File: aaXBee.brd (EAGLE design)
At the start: 100 x 80 mm, 67 parts, among them Q1 IRLML6244TR, U1 MCP1640C, U2 ATmega328P-AU, U3 DS3232, X1 XB24-Z7WIT-004, Y2 8MHz

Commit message: First reasonably complete routing.
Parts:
- removed C10: 27pF, _jc:M0805
- removed D2: Green, adafruit:CHIPLED_1206
- removed JMP1: solder jumper, _jc:M0805
- removed JP4: RTC BACKUP, SparkFun:1X03_LOCK
- removed R8: 1K, _jc:M0805
- removed S1: RESET, _jc:SWITCH-TACT-6X3.5-SMT
- removed U3: DS3232, _jc:SO20W
- removed X1: XB24-Z7WIT-004, _jc:XBEE_OVAL_PADS
- removed Y2: 8MHz, _jc:CRYSTAL-ABRACON-ABM2
- added A1: XB24-Z7WIT-004, _jc:XBEE_OVAL_PADS
- added B2: 2xAA, _jc:KEYSTONE-2462-NO-HOLES
- added C12, C13: 100nF, _jc:M0805
- added C14, C16: 27pF, _jc:M0805
- added L2: 10uH, _jc:M0805
- added L3: 4.7uH, _jc:NRS4018
- added PR14, PR15, PR16, PR17: PROTO-10, _jc:PROTO-10
- added R16: 562K, _jc:M0805
- added R17: 249K, _jc:M0805
- added SJ1: 5V, jumper:SJ
- added SJ2: (no value), jumper:SJ_2
- added SJ3: 3V3, jumper:SJ
- added SW1: (no value), _jc:SWITCH-TACT-6X3.5-SMT
- added SW2: RESET, _jc:SWITCH-TACT-6X3.5-SMT
- added U4: ATmega328P-AU, atmel:TQFP32-08
- added U5: MCP9808, _jc:MSOP8
- added U6: DS3231, _jc:SO-16DW
- added Y1: 8MHz, _jc:CRYSTAL-ABRACON-ABM2
- C15: value 10uF -> 100nF; device _jc:C0805 -> _jc:M0805
- C6, C7: value 100nF -> 10uF
- C9: value 27pF -> 100nF
- D1: value Red -> Yellow; device adafruit:CHIPLED_1206 -> _jc:D0805
- D7, D8: device adafruit:CHIPLED_0805 -> _jc:D0805
- R13, R14, R15: device _jc:R0805 -> _jc:M0805
- R3: value 249K -> 976K
- U1: value MCP1640C -> MCP1640D
- U2: value ATmega328P-AU -> MCP1640D; device atmel:TQFP32-08 -> _jc:SOT23-6
- moved LOGO1 170.6 mm to (90.2, 68.6)
- moved U$2 162.3 mm to (96.5, 30.5), turned to 90 degrees
- moved PR13 161.4 mm to (86.4, 57.1)
- moved JP6 149.6 mm to (63.5, 3.81)
- moved PR2 145.5 mm to (82.5, 21.6)
- moved PR12 143.4 mm to (82.5, 47.0)
- moved PR10 143.0 mm to (82.5, 44.5)
- moved PR8 142.6 mm to (82.5, 41.9)
- moved PR6 142.2 mm to (82.5, 39.4)
- moved PR4 141.8 mm to (82.5, 36.8)
- moved R5 140.7 mm to (57.1, 27.9), turned to 270 degrees
- moved C4 139.4 mm to (59.7, 27.9), turned to 270 degrees
- moved Q1 138.6 mm to (80.0, 3.81), turned to 270 degrees
- moved C5 136.1 mm to (49.5, 17.4), turned to 270 degrees
- moved R12 133.0 mm to (74.9, 3.81), turned to 180 degrees
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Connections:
- removed net LED2: R8.2, U2.12
- removed net N$11: C10.1, U2.8, Y2.P$1
- removed net N$3: D2.A, R8.1
- removed net N$39: R14.2, X1.6
- removed net N$40: R15.2, X1.15
- new net AREF: C13.1, JP1.1, U4.20
- new net ASC: A1.15, R15.2
- new net CTS: A1.12, U4.9
- new net N$43: C14.1, U4.7, Y1.P$2
- new net N$44: C16.1, U4.8, Y1.P$1
- new net N$46: C12.1, L2.2, U4.18
- new net RSSI: A1.6, R14.2
- new net SLP: A1.9, U4.10
- new net SW1: SW1.P$1, U4.12
- net +3V3: now also C7.1, R3.1, SJ2.1, U2.5; no longer C15.1, R13.1, X1.1
- net /RESET: now also SW2.P$1, U4.29; no longer S1.P$1, U2.29
- net /SS: now also JP1.12, U4.14; no longer JP1.9, U2.14
- net 32KHZ: now also U6.1; no longer JP1.1, U3.3
- net ADC0: now also U4.23; no longer U2.23
- net ADC1: now also U4.24; no longer U2.24
- net ADC2: now also U4.25; no longer U2.25
- net ADC3: now also U4.26; no longer U2.26
- net ADC6: now also U4.19; no longer U2.19
- net ADC7: now also U4.22; no longer U2.22
- net BAT: now also B2.POS, C6.1, L3.P$1, U2.6; no longer JP4.1
- net EN: now also U2.3, U4.2; no longer U2.2
- net GND: now also A1.10, B2.NEG, C12.2, C13.2, C14.2, C16.2, D1.K, D7.K, D8.K, R16.2, R17.2, SJ1.2, SW1.P$2, SW2.P$2, U2.2, U4.21, U4.3, U4.5, U5.4, U5.5, U5.6, U5.7, U6.10, U6.11, U6.12, U6.13, U6.5, U6.6, U6.7, U6.8, U6.9; no longer C10.2, D1.C, D2.C, D7.C, D8.C, JMP1.2, R3.2, S1.P$2, U2.21, U2.3, U2.5, U3.1, U3.10, U3.11, U3.12, U3.13, U3.14, U3.15, U3.19, U3.2, U3.7, U3.8, U3.9, X1.10
- net INT: now also U4.1, U6.3; no longer U2.1, U3.5
- net LED1: now also U4.11; no longer U2.11
- net MISO: now also JP1.10, U4.16; no longer JP1.11, U2.16
- net MOSI: now also JP1.11, U4.15; no longer JP1.12, U2.15
- net N$1: now also U6.14; no longer JP4.3
- net N$12: now also R16.1, R3.2, U2.4; no longer JMP1.1, R2.2, R3.1
- net N$13: now also L3.P$2, U2.1; no longer C8.1, U2.20
- net N$35: now also A1.1, C15.1, C3.1, R13.1, SJ2.2; no longer JP4.2, U3.16
- net N$37: now also A1.3, SJ3.1; no longer X1.3
- net N$38: now also A1.2; no longer X1.2
- net N$8: now also R17.1, R2.2, SJ1.1; no longer C9.1, U2.7, Y2.P$2
- net PPWR: now also C9.1, U4.32, U5.8, U6.2; no longer U2.32, U3.4
- net RXD: now also U4.30; no longer U2.30
- net SCK: now also JP1.9, U4.17; no longer JP1.10, U2.17
- net SCL: now also R10.2, U4.28, U5.2, U6.16; no longer R10.1, U2.28, U3.18
- net SDA: now also R9.2, U4.27, U5.1, U6.15; no longer R9.1, U2.27, U3.17
- net SPWR: now also U4.13; no longer U2.13
- net TXD: now also SJ3.2, U4.31; no longer U2.31
- net VCC: now also C8.1, L2.1, R10.1, R9.1, SJ2.3, U4.4, U4.6; no longer C3.1, C6.1, C7.1, R10.2, R9.2, U2.18, U2.4, U2.6
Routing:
- net VCC: track 0.00 -> 86.0 mm, vias 0 -> 9
- net BAT: track 0.00 -> 80.2 mm, vias 0 -> 1
- net /RESET: track 0.00 -> 60.1 mm, vias 0 -> 2
- net SDA: track 0.00 -> 54.5 mm, vias 0 -> 3
- net SPWR: track 0.00 -> 53.5 mm, vias 0 -> 2
- net SCK: track 0.00 -> 49.0 mm
- net EN: track 0.00 -> 48.7 mm, vias 0 -> 3
- net SCL: track 0.00 -> 48.6 mm, vias 0 -> 2
- net SGND: track 0.00 -> 47.2 mm
- net RXD: track 0.00 -> 45.3 mm, vias 0 -> 1
- net TXD: track 0.00 -> 43.2 mm, vias 0 -> 1
- net MISO: track 0.00 -> 41.6 mm
- net SLP: track 0.00 -> 39.9 mm, vias 0 -> 1
- net MOSI: track 0.00 -> 38.0 mm
- net ADC7: track 0.00 -> 37.7 mm, vias 0 -> 3
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- added copper zone on layer 1, net GND
- added copper zone on layer 16, net VCC
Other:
- board size 100 x 80 mm -> 99.1 x 61 mm
- board text added: "+3V-"

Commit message: Routing complete.
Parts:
- removed JP1: PROTO-12NR, _jc:PROTO-12-NR
- removed U$1, U$2: PROTO-12PROTO, _jc:PROTO-12
- added PR18, PR19: (no value), _jc:PROTO-16
- added PR20: (no value), _jc:PROTO-14-NR
- added SJ4: 5V, jumper:SJ
- SJ3: value 3V3 -> /5V
- moved R4 23.6 mm to (12.3, 55.9)
- moved TB1 17.4 mm to (6.60, 49.1)
- moved D1 12.8 mm to (58.4, 3.81)
- moved R7 12.8 mm to (58.4, 8.89)
- moved SW2 11.9 mm to (45.2, 6.48)
- moved R10 11.4 mm to (66.0, 55.9)
- moved B1 11.4 mm to (29.2, 50.8)
- moved C11 11.4 mm to (55.9, 55.9)
- moved C9 11.4 mm to (58.4, 55.9)
- moved R9 11.4 mm to (68.6, 55.9)
- moved U5 11.4 mm to (62.2, 55.9)
- moved U6 11.4 mm to (48.3, 53.3)
- moved D4 6.35 mm to (27.9, 14.0), turned to 90 degrees
- moved C5 4.73 mm to (44.8, 16.9), turned to 180 degrees
- moved R6 3.82 mm to (48.6, 16.0)
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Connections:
- net +3V3 renamed N$39
- net N$35 renamed XBEE_SUPPLY
- removed net LED1: R7.2, U4.11
- removed net SW1: SW1.P$1, U4.12
- new net N$35: C6.1, L3.P$1, SJ4.2, U2.6
- new net N$40: PR14.1, PR14.2, PR14.3, PR14.4, PR14.5
- new net N$45: PR14.10, PR14.6, PR14.7, PR14.8, PR14.9
- new net N$47: PR15.1, PR15.2, PR15.3, PR15.4, PR15.5
- new net N$48: PR15.10, PR15.6, PR15.7, PR15.8, PR15.9
- new net N$49: PR16.1, PR16.2, PR16.3, PR16.4, PR16.5
- new net N$50: PR16.10, PR16.6, PR16.7, PR16.8, PR16.9
- new net N$51: PR17.1, PR17.2, PR17.3, PR17.4, PR17.5
- new net N$52: PR17.10, PR17.6, PR17.7, PR17.8, PR17.9
- new net PB0: R7.2, U4.12
- new net PD7: SW1.P$1, U4.11
- net /SS: now also PR20.3; no longer JP1.12
- net ADC0: now also PR20.9; no longer JP1.7
- net ADC1: now also PR20.10; no longer JP1.6
- net ADC2: now also PR20.11; no longer JP1.5
- net ADC3: now also PR20.12; no longer JP1.4
- net ADC6: now also PR20.7; no longer JP1.8
- net AREF: now also PR20.8; no longer JP1.1
- net BAT: now also SJ4.1; no longer C6.1, L3.P$1, U2.6
- net MISO: now also PR20.5; no longer JP1.10
- net MOSI: now also PR20.4; no longer JP1.11
- net SCK: now also PR20.6; no longer JP1.9
- net SCL: now also PR20.14; no longer JP1.2
- net SDA: now also PR20.13; no longer JP1.3
- net SGND: now also PR18.1, PR18.10, PR18.11, PR18.12, PR18.13, PR18.14, PR18.15, PR18.16, PR18.2, PR18.3, PR18.4, PR18.5, PR18.6, PR18.7, PR18.8, PR18.9; no longer U$2.1, U$2.10, U$2.11, U$2.12, U$2.2, U$2.3, U$2.4, U$2.5, U$2.6, U$2.7, U$2.8, U$2.9
- net VCC: now also PR19.1, PR19.10, PR19.11, PR19.12, PR19.13, PR19.14, PR19.15, PR19.16, PR19.2, PR19.3, PR19.4, PR19.5, PR19.6, PR19.7, PR19.8, PR19.9; no longer U$1.1, U$1.10, U$1.11, U$1.12, U$1.2, U$1.3, U$1.4, U$1.5, U$1.6, U$1.7, U$1.8, U$1.9
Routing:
- net PD7: track 0.00 -> 32.3 mm
- net PB0: track 0.00 -> 28.9 mm
- net ADC7: track 37.7 -> 65.5 mm
- net N$35: track 0.00 -> 26.6 mm
- net SW1: track 25.5 -> 0.00 mm, vias 2 -> 0
- net LED1: track 22.7 -> 0.00 mm, vias 2 -> 0
- net BAT: track 80.2 -> 61.5 mm, vias 1 -> 0
- net N$52: track 0.00 -> 10.2 mm
- net N$50: track 0.00 -> 10.2 mm
- net N$48: track 0.00 -> 10.2 mm
- net N$45: track 0.00 -> 10.2 mm
- net N$51: track 0.00 -> 10.2 mm
- net N$49: track 0.00 -> 10.2 mm
- net N$47: track 0.00 -> 10.2 mm
- net N$40: track 0.00 -> 10.2 mm
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
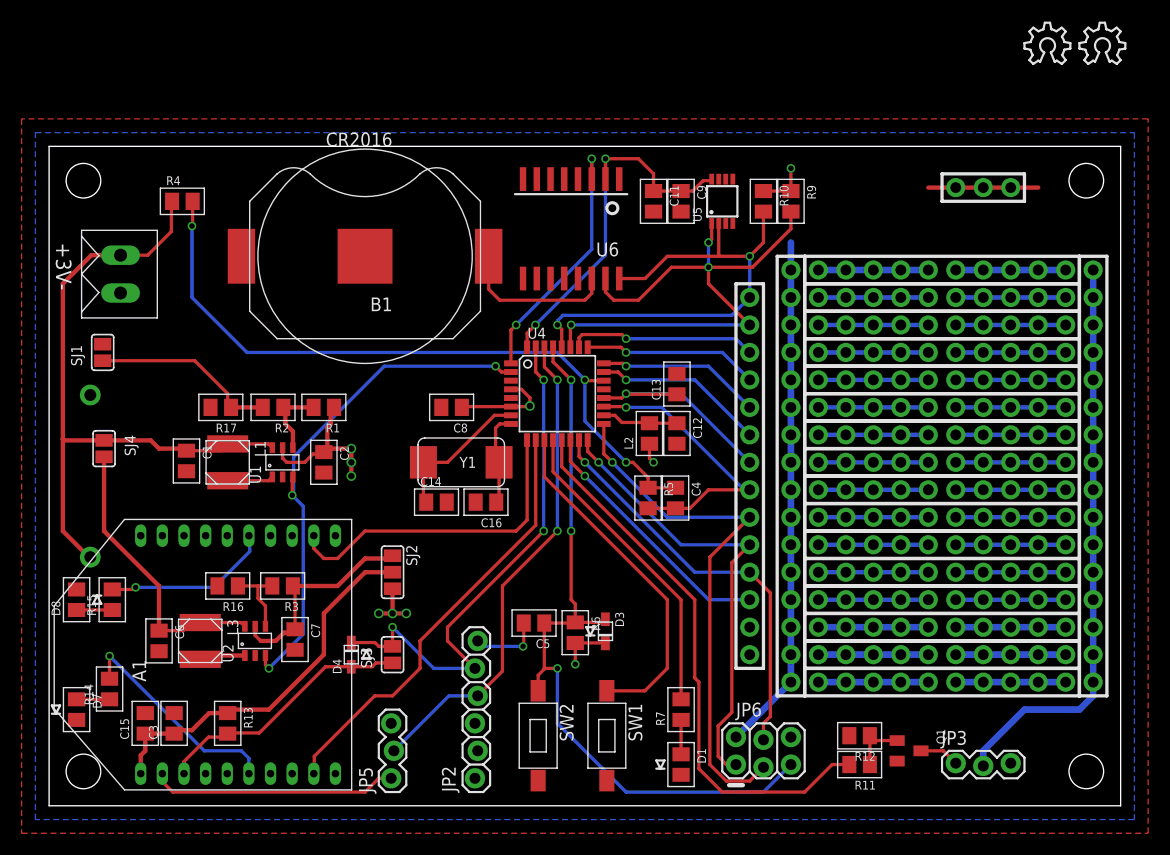
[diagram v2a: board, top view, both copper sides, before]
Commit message: Tweak a few traces.
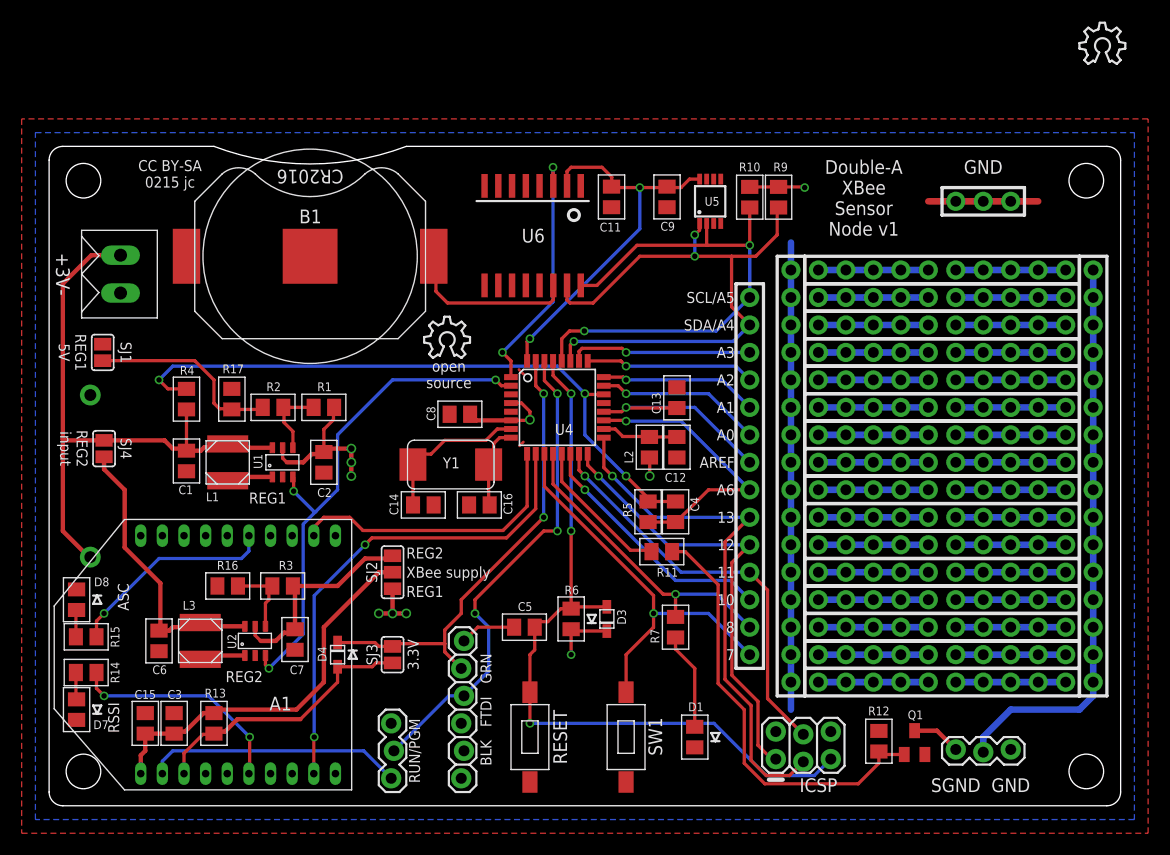
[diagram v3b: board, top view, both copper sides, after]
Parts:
- D1, D7: device _jc:D0805 -> _jc:D0805A
- JP6: value (none) -> ICSP
- PR18: value (none) -> Proto ground
- PR19: value (none) -> Proto Vcc
- PR20: value (none) -> Signals
- SJ2: value (none) -> XBee VR Sel
- SW1: value (none) -> SW1
- moved LOGO1 61.8 mm to (34.7, 41.4)
- moved R11 26.9 mm to (56.6, 23.5)
- moved R4 18.3 mm to (12.7, 37.6), turned to 90 degrees
- moved R7 7.64 mm to (57.9, 16.5)
- moved B1 5.08 mm to (24.1, 50.8)
- moved R15 4.19 mm to (3.43, 15.6), turned to 0 degrees
- moved C11 3.91 mm to (52.0, 56.3)
- moved JP6 3.72 mm to (67.2, 4.32)
- moved U6 3.61 mm to (44.7, 52.7)
- moved D1 2.84 mm to (59.7, 6.35)
- moved R14 2.64 mm to (3.43, 12.3), turned to 0 degrees
- moved R12 1.85 mm to (76.7, 5.97), turned to 90 degrees
- moved SW1 1.78 mm to (53.3, 6.35)
- moved C9 1.36 mm to (57.1, 56.3)
- moved R10 1.33 mm to (64.8, 56.3)
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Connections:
- net PB0: now also PR20.2
- net PD7: now also PR20.1
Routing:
- net SPWR: track 51.5 -> 13.5 mm
- net N$24: track 5.37 -> 40.8 mm
- net TXD: track 49.7 -> 43.3 mm, vias 3 -> 2
- net PD7: track 32.3 -> 38.3 mm, vias 0 -> 1
- net N$2: track 3.18 -> 9.00 mm
- net SLP: track 40.3 -> 45.4 mm, vias 0 -> 2
- net ADC7: track 65.5 -> 60.5 mm
- net BAT: track 61.5 -> 56.9 mm
- net ASC: track 15.7 -> 19.6 mm
- net VCC: track 87.7 -> 84.2 mm
- net CTS: track 30.2 -> 27.2 mm
- net SCL: track 45.7 -> 48.5 mm
- net SDA: track 52.7 -> 55.2 mm
- net N$1: track 14.6 -> 16.1 mm
- net RST: track 6.59 -> 5.16 mm, vias 1 -> 0
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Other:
- outline, holes or cut-outs redrawn
- board text added: "10"
- board text added: "11"
- board text added: "12"
- board text added: "13"
- board text added: "3.3V"
- board text added: "7"
- board text added: "8"
- board text added: "A0"
- board text added: "A1"
- board text added: "A2"
- board text added: "A3"
- board text added: "A6"
- board text added: "AREF"
- board text added: "ASC"
- board text added: "BLK FTDI GRN"
- board text added: "CC BY-SA 0215 jc"
- board text added: "Double-A XBee Sensor Node v1"
- board text added: "GND"
- board text added: "ICSP"
- board text added: "REG1"
- board text added: "REG1 5V"
- board text added: "REG2"
- board text added: "REG2 input"
- board text added: "RESET"
- board text added: "RSSI"
- board text added: "RUN/PGM"
- board text added: "SCL/A5"
- board text added: "SDA/A4"
- board text added: "SGND"
- board text added: "XBee supply"
- board text added: "open source"
